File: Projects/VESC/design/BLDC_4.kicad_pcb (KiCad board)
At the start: 4 copper layers, 123 parts, among them P10 AMP17614426-2_EDGE, Q1 IRFS7530, Q2 IRFS7530, Q3 IRFS7530, Q4 IRFS7530, Q5 IRFS7530, Q6 IRFS7530, U1 STM32F40X_LQFP64, U2 TC2117, U3 DRV8302, U401 SN65HVD232, X2 CRYSTAL_GROUND_PIN

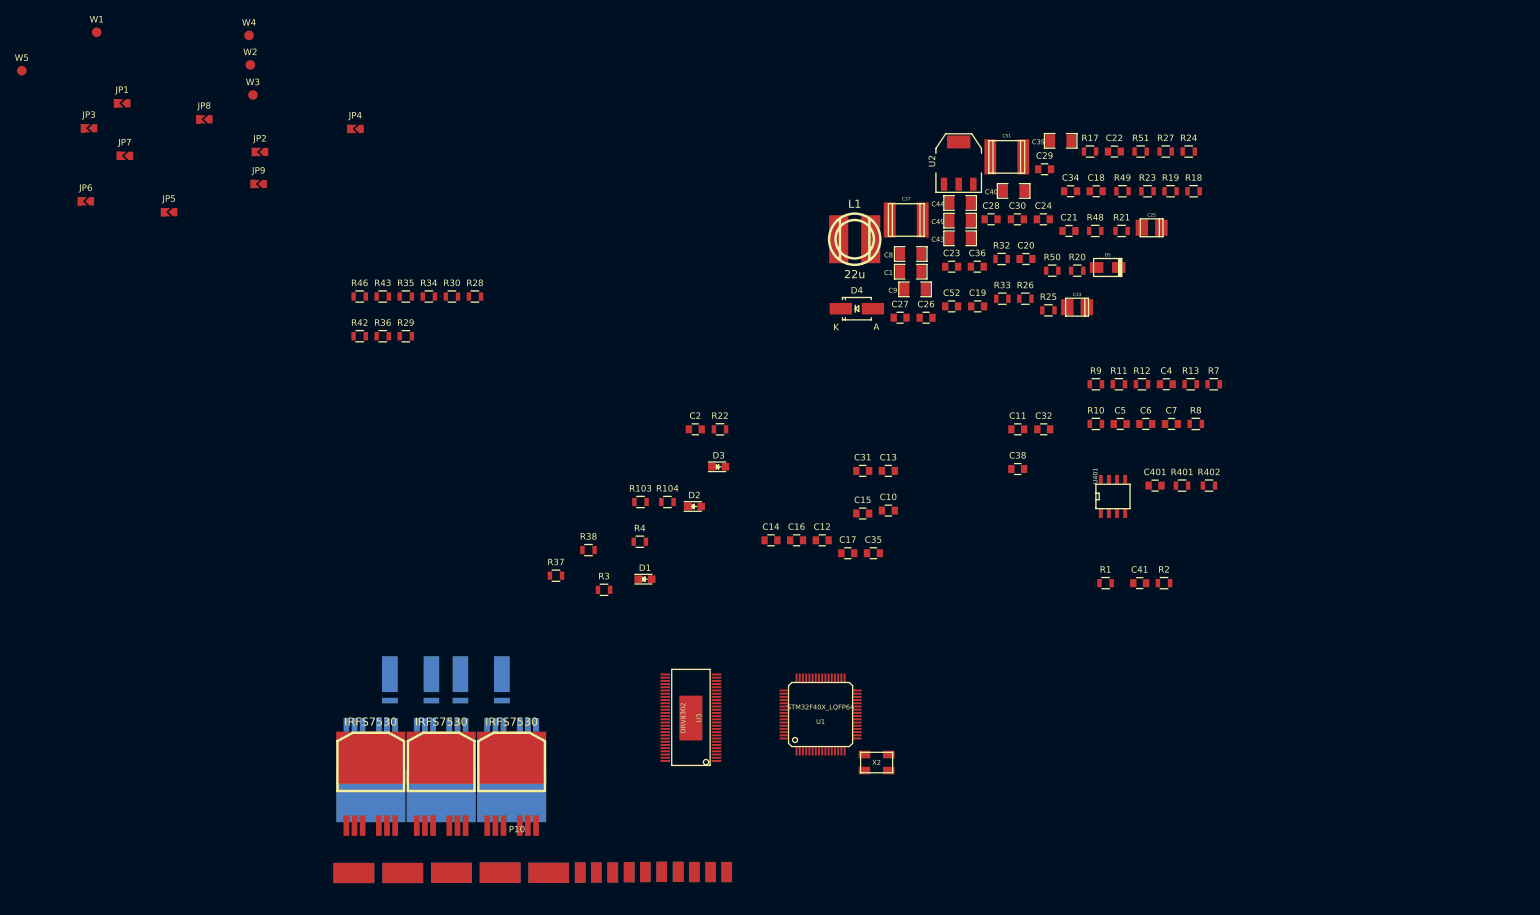
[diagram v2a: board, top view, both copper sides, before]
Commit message: VESC MOSFET layout
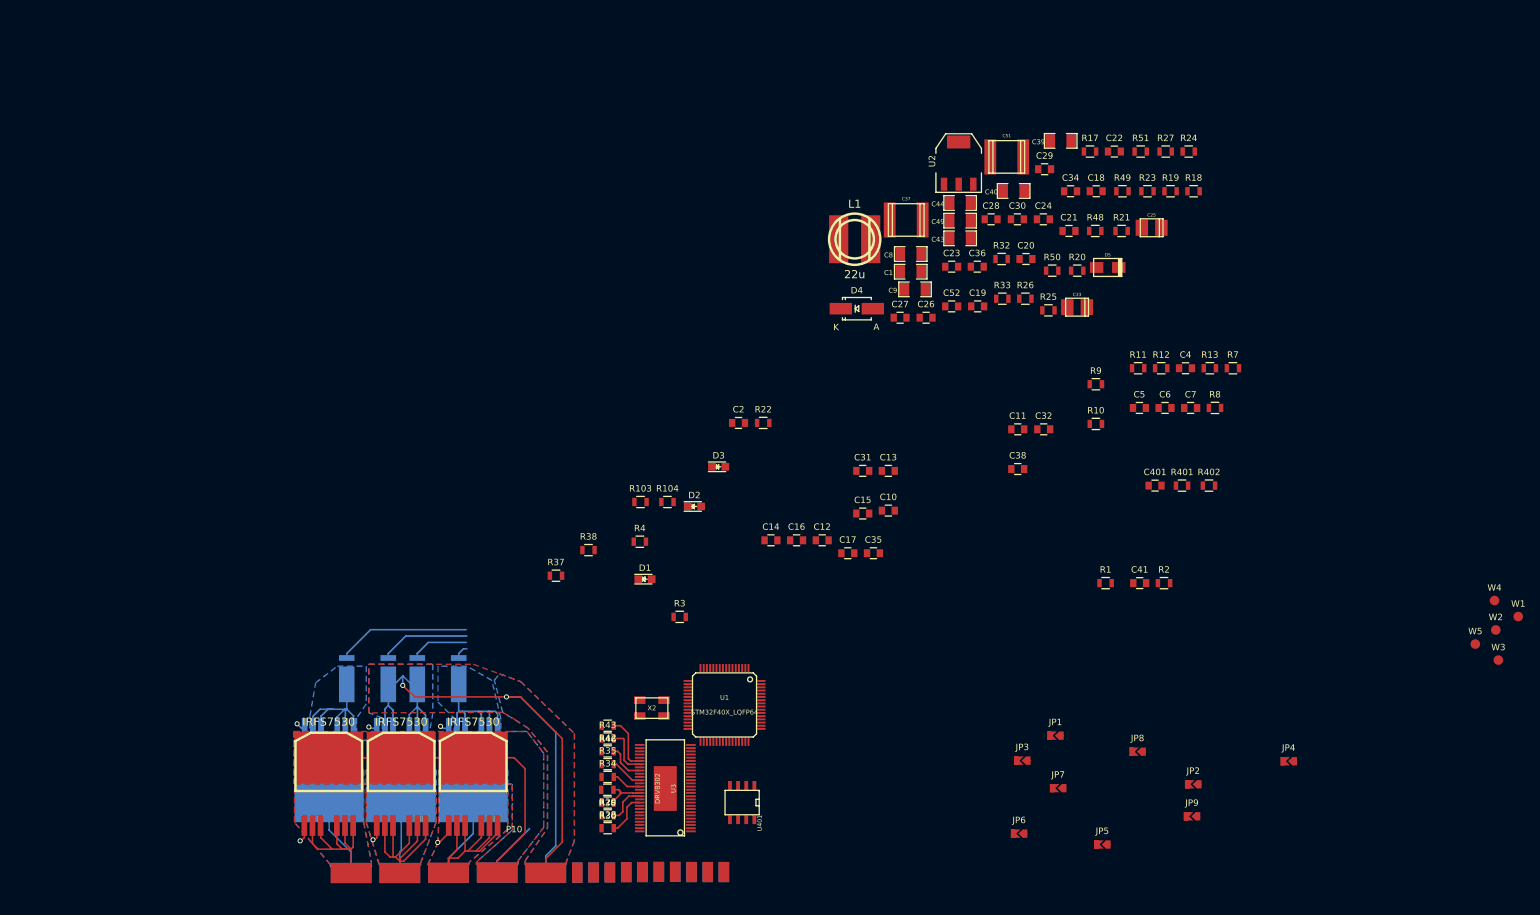
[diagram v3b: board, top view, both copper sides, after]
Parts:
- moved W5 244.0 mm to (249.5, 109.2)
- moved W1 240.0 mm to (256.2, 105.0)
- moved W2 213.6 mm to (252.7, 107.0)
- moved W3 213.6 mm to (253.1, 111.8)
- moved W4 213.6 mm to (252.5, 102.5)
- moved JP1 176.1 mm to (183.9, 123.5)
- moved JP2 176.1 mm to (205.4, 131.2)
- moved JP3 176.1 mm to (178.8, 127.5)
- moved JP4 176.1 mm to (220.3, 127.5)
- moved JP5 176.1 mm to (191.2, 140.6)
- moved JP6 176.1 mm to (178.2, 138.8)
- moved JP7 176.1 mm to (184.3, 131.8)
- moved JP8 176.1 mm to (196.8, 126.0)
- moved JP9 176.1 mm to (205.2, 136.2)
- moved R28 85.6 mm to (114.0, 138.0)
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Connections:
- net /CAN bus transceiver/CANH renamed /CAN_H
- net /CAN bus transceiver/CANL renamed /CAN_L
- net /CardEdge/CS renamed /CS
- net /CardEdge/H1 renamed /H1
- net /CardEdge/H2 renamed /H2
- net /CardEdge/H3 renamed /H3
- net /CardEdge/USB_DM renamed /USB_DM
- net /CardEdge/USB_DP renamed /USB_DP
- net /Filters/TEMP_IN renamed /Temp
- net /MCU/HALL_2 renamed /MISO
- net /MCU/HALL_3 renamed /SCK
- net /MCU/MISO_ADC_EXT2 renamed /MISO_2
- net /MCU/RX_SCL_MOSI renamed /RX_SCL_MOSI
- net /MCU/SCK_ADC_EXT renamed /SCK_2
- net /MCU/TX_SDA_NSS renamed /TX_SDA
- net /Mosfet driver/H1_VS renamed /W
- net /Mosfet driver/H2_VS renamed /X
- net /Mosfet driver/H3_VS renamed /Y
- U1 pad 11: Net-(U1-Pad11) -> (no net)
- U1 pad 2: Net-(U1-Pad2) -> (no net)
- U1 pad 28: Net-(U1-Pad28) -> (no net)
- U1 pad 3: Net-(U1-Pad3) -> (no net)
- U1 pad 39: Net-(U1-Pad39) -> (no net)
- U1 pad 4: Net-(U1-Pad4) -> (no net)
- U1 pad 40: Net-(U1-Pad40) -> (no net)
- U1 pad 50: Net-(U1-Pad50) -> (no net)
- U1 pad 54: Net-(U1-Pad54) -> (no net)
- U1 pad 55: Net-(U1-Pad55) -> (no net)
- U1 pad 56: Net-(U1-Pad56) -> (no net)
- U1 pad 57: /MCU/SERVO -> (no net)
- U1 pad 9: Net-(U1-Pad9) -> (no net)
- U3 pad 4: Net-(U3-Pad4) -> (no net)
- U3 pad 5: Net-(U3-Pad5) -> (no net)
- U3 pad 55: Net-(U3-Pad55) -> (no net)
- U3 pad 56: Net-(U3-Pad56) -> (no net)
- U401 pad 1: /CAN bus transceiver/CAN_TX -> /CAN bus transceiver/CAN_RX
- U401 pad 4: /CAN bus transceiver/CAN_RX -> /CAN bus transceiver/CAN_TX
- U401 pad 5: Net-(U401-Pad5) -> (no net)
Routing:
- net GND: track 0.00 -> 132.5 mm, vias 0 -> 2
- net V_SUPPLY: track 0.00 -> 58.4 mm
- net Net-(Q2-PadG): track 0.00 -> 57.3 mm, vias 0 -> 1
- net Net-(Q1-PadG): track 0.00 -> 55.9 mm, vias 0 -> 1
- net /X: track 0.00 -> 45.9 mm
- net /Y: track 0.00 -> 45.6 mm
- net Net-(Q3-PadG): track 0.00 -> 45.1 mm, vias 0 -> 1
- net Net-(Q4-PadG): track 0.00 -> 44.6 mm, vias 0 -> 1
- net /W: track 0.00 -> 44.0 mm
- net Net-(Q5-PadG): track 0.00 -> 34.1 mm, vias 0 -> 1
- net Net-(Q6-PadG): track 0.00 -> 32.6 mm, vias 0 -> 1
- net /Mosfet driver/H3_LOW: track 0.00 -> 32.4 mm
- net /Mosfet driver/H1_LOW: track 0.00 -> 32.0 mm
- net /Mosfet driver/SH2_A: track 0.00 -> 20.9 mm
- net /Mosfet driver/SH2_B: track 0.00 -> 14.1 mm
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- added copper zone on B.Cu, net /Mosfet driver/H1_LOW
- added copper zone on B.Cu, net /Mosfet driver/H3_LOW
- added copper zone on B.Cu, net /W
- added copper zone on F.Cu, net /W
- added copper zone on B.Cu, net /X
- added copper zone on F.Cu, net /X
- added copper zone on B.Cu, net /Y
- added copper zone on F.Cu, net /Y
- added copper zone on B.Cu, net GND
- added copper zone on F.Cu, net GND
- added copper zone on GND, net GND
- added copper zone on GND2, net GND
- added copper zone on B.Cu, net V_SUPPLY
- added copper zone on F.Cu, net V_SUPPLY

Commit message: completing VESC card layout
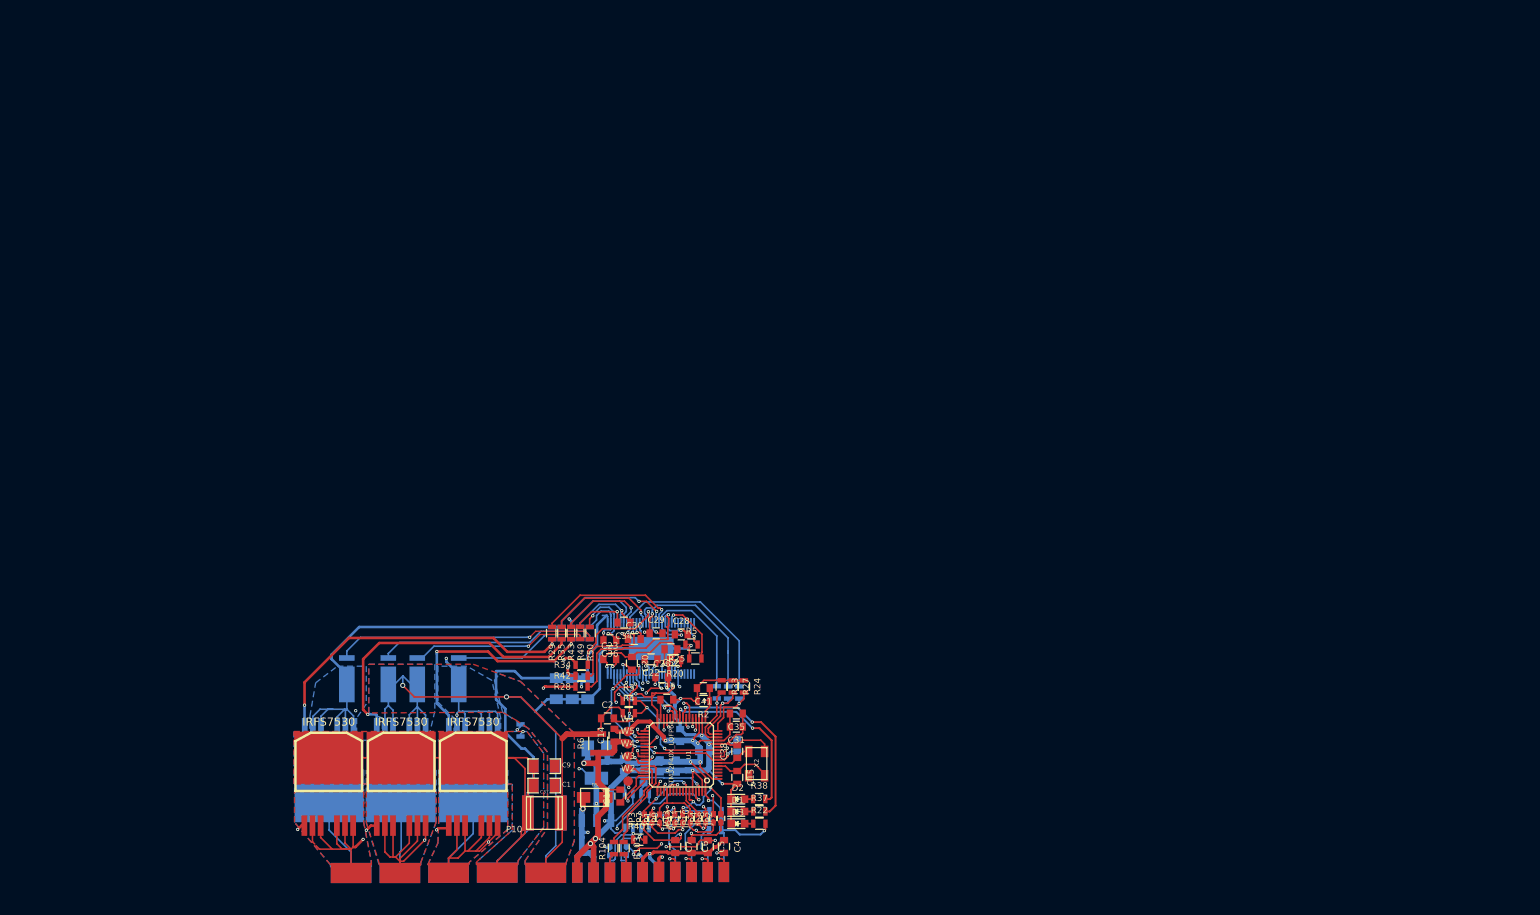
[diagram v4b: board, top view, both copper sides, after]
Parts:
- removed C18: 2.2u, Capacitors_SMD:C_0805
- removed C19: 120p, Capacitors_SMD:C_0805
- removed C21: 6.8n, Capacitors_SMD:C_0805
- removed C27: 100n, Capacitors_SMD:C_0805
- removed C33: 100u, w_smd_cap:c_tant_B
- removed C39: 10u,50V, CRF1:SMD-1206
- removed D4: DIODESCH, Diodes_SMD:SMA_Handsoldering
- removed L1: 22u, w_smd_inductors:inductor_smd_8x5mm
- removed R17: 18k, Resistors_SMD:R_0805
- removed R18: 3k3, Resistors_SMD:R_0805
- removed R19: 15k, Resistors_SMD:R_0805
- removed R21: 220k, Resistors_SMD:R_0805
- removed R402: 10k, Resistors_SMD:R_0805
- added JP10: Jumper_NC_Small, USST-footprints:J_0603, F.Cu at (128.1, 136.5)
- added JP11: Jumper_NC_Small, USST-footprints:J_0603, F.Cu at (126.9, 136.5)
- added JP12: Jumper_NC_Small, USST-footprints:J_0603, F.Cu at (125.7, 136.5)
- added JP13: Jumper_NC_Small, USST-footprints:J_0603, F.Cu at (124.5, 136.5)
- added R5: 1k, Resistors_SMD:R_0805, F.Cu at (127.1, 109.3)
- added R6: 0, Resistors_SMD:R_1210, F.Cu at (112.5, 124.8)
- C10, C11, C12, C13, C24, C25, C32, C40, C401, C43, C44, C49, C51, C8, R1, R10, R11, R12, R13, R23, R26, R30, R32, R36, R46, R48, R51, R7, R8, R9, U2, U3: moved to B.Cu
- JP1, JP2, JP3, JP4, JP7, JP8, JP9: footprint USST-footprints:J_0805 -> USST-footprints:J_0603
- JP5, JP6: footprint USST-footprints:J_0805 -> USST-footprints:J_0603; moved to B.Cu
- U401: value SN65HVD232 -> MCP2562FD; moved to B.Cu
- moved W1 140.2 mm to (117.1, 122.9)
- moved W2 137.5 mm to (117.2, 130.7)
- moved W4 137.5 mm to (117.1, 126.8)
- moved W3 137.0 mm to (117.2, 128.7)
- moved W5 133.3 mm to (117.1, 124.8)
- moved C51 125.3 mm to (104.1, 135.6)
- moved C25 118.7 mm to (112.4, 125.6)
- moved C40 118.3 mm to (104.1, 131.3), turned to 180 degrees
- moved D5 115.2 mm to (112.0, 133.2)
- moved U2 114.3 mm to (112.2, 133.5), turned to 180 degrees
- moved R51 114.3 mm to (111.2, 107.5), turned to 90 degrees
- moved R49 109.2 mm to (109.7, 107.5), turned to 90 degrees
- moved R7 109.1 mm to (132.2, 140.9), turned to 90 degrees
- moved R24 108.6 mm to (135.3, 115.9), turned to 270 degrees
- moved R8 108.6 mm to (124.6, 140.9), turned to 90 degrees
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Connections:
- net /MCU/USB_DM renamed /USBD_N
- net /MCU/USB_DP renamed /USBD_P
- net /USB_DM renamed /USB_N
- net /USB_DP renamed /USB_P
- C10 pad 1: GND -> GNDD
- C11 pad 1: GND -> GNDD
- C12 pad 1: GND -> GNDD
- C13 pad 1: GND -> GNDD
- C14 pad 1: GND -> GNDD
- C15 pad 2: GND -> GNDD
- C16 pad 2: GND -> GNDD
- C17 pad 2: GND -> GNDD
- C20 pad 1: GND -> GNDD
- C23 pad 1: GND -> GNDD
- C24 pad 2: GND -> GNDD
- C25 pad 2: GND -> GNDD
- C26 pad 2: GND -> GNDD
- C31 pad 1: GND -> GNDD
- C32 pad 1: GND -> GNDD
- C35 pad 1: GND -> GNDD
- C38 pad 2: GND -> GNDD
- C4 pad 1: GND -> GNDD
- C401 pad 1: VCC -> +5V
- C401 pad 2: GND -> GNDD
- C41 pad 2: GND -> GNDD
- C5 pad 2: GND -> GNDD
- C52 pad 1: GND -> GNDD
- C6 pad 2: GND -> GNDD
- C7 pad 2: GND -> GNDD
- D1 pad 1: GND -> GNDD
- D2 pad 1: GND -> GNDD
- D3 pad 1: GND -> GNDD
- D5 pad 1: GND -> +5V
- D5 pad 2: +5V -> GNDD
- JP4 pad 1: /CS -> /CardEdge/CS
- JP7 pad 1: /MISO -> /CardEdge/MISO
- JP8 pad 1: /SCK -> /CardEdge/SCK
- JP9 pad 1: /RX_SCL_MOSI -> /CardEdge/MOSI
- JP9 pad 2: VCC -> /RX_SCL_MOSI
- P10 pad 11: GND -> GNDD
- P10 pad 16: /CS -> /CardEdge/CS
- P10 pad 17: /SCK -> /CardEdge/SCK
- P10 pad 18: /MISO -> /CardEdge/MISO
- P10 pad 19: VCC -> /CardEdge/MOSI
- P10 pad 21: GND -> GNDD
- P10 pad 24: GND -> GNDD
- P10 pad 25: GND -> GNDD
- R2 pad 2: GND -> GNDD
- R20 pad 2: GND -> GNDD
- R24 pad 1: GND -> GNDD
- R27 pad 1: GND -> GNDD
- R33 pad 1: GND -> GNDD
- U1 pad 12: GND -> GNDD
- U1 pad 18: GND -> GNDD
- U1 pad 60: GND -> GNDD
- U1 pad 63: GND -> GNDD
- U2 pad 1: GND -> GNDD
- U3 pad 1: Net-(R21-Pad2) -> (no net)
- U3 pad 10: GND -> GNDD
- U3 pad 2: Net-(C19-Pad2) -> (no net)
- U3 pad 28: GND -> GNDD
- U3 pad 3: Net-(R17-Pad2) -> (no net)
- U3 pad 50: Net-(C27-Pad1) -> (no net)
- U3 pad 51: Net-(C27-Pad1) -> (no net)
- U3 pad 52: Net-(C27-Pad2) -> (no net)
- U3 pad 53: V_SUPPLY -> (no net)
- U3 pad 54: V_SUPPLY -> (no net)
- U3 pad 55: (no net) -> Net-(R5-Pad2)
- U3 pad 8: GND -> GNDD
- U401 pad 1: /CAN bus transceiver/CAN_RX -> /CAN bus transceiver/CAN_TX
- U401 pad 2: GND -> GNDD
- U401 pad 3: VCC -> +5V
- U401 pad 4: /CAN bus transceiver/CAN_TX -> /CAN bus transceiver/CAN_RX
- U401 pad 5: (no net) -> VCC
- U401 pad 8: Net-(R402-Pad1) -> GNDD
- W5 pad 1: GND -> GNDD
- X2 pad 3: GND -> GNDD
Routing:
- net GNDD: track 0.00 -> 224.3 mm, vias 0 -> 14
- net VCC: track 0.00 -> 163.4 mm, vias 0 -> 16
- net /W: track 44.0 -> 143.3 mm, vias 0 -> 2
- net /X: track 45.9 -> 133.5 mm, vias 0 -> 3
- net V_SUPPLY: track 58.4 -> 143.2 mm, vias 0 -> 2
- net /Y: track 45.6 -> 120.8 mm, vias 0 -> 3
- net /Mosfet driver/H1_LOW: track 32.0 -> 89.0 mm, vias 0 -> 2
- net GND: track 132.5 -> 188.7 mm, vias 2 -> 3
- net /TX_SDA: track 0.00 -> 47.8 mm, vias 0 -> 5
- net (no net): track 0.00 -> 46.7 mm, vias 0 -> 1
- net +5V: track 0.00 -> 44.6 mm, vias 0 -> 4
- net /MCU/ADC_TEMP: track 0.00 -> 38.7 mm, vias 0 -> 2
- net /RX_SCL_MOSI: track 0.00 -> 38.1 mm, vias 0 -> 6
- net /Mosfet driver/H3_LOW: track 32.4 -> 67.8 mm, vias 0 -> 3
- net /MCU/LED_GREEN: track 0.00 -> 30.5 mm, vias 0 -> 2
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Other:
- net class Default: clearance 0.1778 -> 0.2032; via_dia 0.8 -> 0.508; via_drill 0.5 -> 0.254
- rule trace_clearance: 0.1778 -> 0.2032
- rule via_min_drill: 0.5 -> 0.254
- rule via_min_size: 0.8 -> 0.508
